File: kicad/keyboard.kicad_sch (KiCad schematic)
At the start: 74 parts, among them SW1 SW_MEC_5G, SW10 SW_MEC_5G, SW11 SW_MEC_5G, SW12 SW_MEC_5G, SW13 SW_MEC_5G, SW14 SW_MEC_5G, SW15 SW_MEC_5G, SW16 SW_MEC_5G, SW17 SW_MEC_5G, SW18 SW_MEC_5G, SW19 SW_MEC_5G, SW2 SW_MEC_5G, SW20 SW_MEC_5G, SW21 SW_MEC_5G, SW22 SW_MEC_5G, SW23 SW_MEC_5G, SW24 SW_MEC_5G, SW25 SW_MEC_5G, SW26 SW_MEC_5G, SW27 SW_MEC_5G, SW28 SW_MEC_5G, SW29 SW_MEC_5G, SW3 SW_MEC_5G, SW30 SW_MEC_5G, SW31 SW_MEC_5G, SW32 SW_MEC_5G, SW33 SW_MEC_5G, SW34 SW_MEC_5G, SW35 SW_MEC_5G, SW36 SW_MEC_5G, SW37 SW_MEC_5G, SW38 SW_MEC_5G, SW39 SW_MEC_5G, SW4 SW_MEC_5G, SW40 SW_MEC_5G, SW41 SW_MEC_5G, SW42 SW_MEC_5G, SW43 SW_MEC_5G, SW44 SW_MEC_5G, SW45 SW_MEC_5G, SW46 SW_MEC_5G, SW47 SW_MEC_5G, SW48 SW_MEC_5G, SW49 SW_MEC_5G, SW5 SW_MEC_5G, SW50 SW_MEC_5G, SW51 SW_MEC_5G, SW52 SW_MEC_5G, SW53 SW_MEC_5G, SW54 SW_MEC_5G, SW55 SW_MEC_5G, SW56 SW_MEC_5G, SW57 SW_MEC_5G, SW58 SW_MEC_5G, SW59 SW_MEC_5G, SW6 SW_MEC_5G, SW60 SW_MEC_5G, SW7 SW_MEC_5G, SW8 SW_MEC_5G, SW9 SW_MEC_5G, U1 MCP23017-E{slash}SO, U2 MCP23017-E{slash}SO, U3 MCP23017-E{slash}SO, U4 MCP23017-E{slash}SO

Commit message: Started on layout
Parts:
- A1: footprint pimoroni-boards_TINY2040 -> footprints:pimoroni-boards-TINY2040
- R2, R3: footprint (none) -> Resistor_SMD:R_0805_2012Metric_Pad1.20x1.40mm_HandSolder
- SW1, SW10, SW11, SW12, SW13, SW14, SW15, SW16, SW17, SW18, SW19, SW2, SW20, SW21, SW22, SW23, SW24, SW25, SW26, SW27, SW28, SW29, SW3, SW30, SW31, SW32, SW33, SW34, SW35, SW36, SW37, SW38, SW39, SW4, SW40, SW41, SW42, SW43, SW44, SW45, SW46, SW47, SW48, SW49, SW5, SW50, SW51, SW52, SW53, SW54, SW55, SW56, SW57, SW58, SW59, SW6, SW60, SW7, SW8, SW9: footprint (none) -> footprints:CherryMX_ChocV2_1u; symbol Switch:SW_MEC_5G -> project_library:SW_KAILH_CHOC_V2
- U1, U2, U3, U4: footprint SOIC127P1030X265-28N -> footprints:SOIC127P1030X265-28N
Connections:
- net GND: now also SW1.2 (B), SW10.2 (B), SW11.2 (B), SW12.2 (B), SW13.2 (B), SW14.2 (B), SW15.2 (B), SW16.2 (B), SW17.2 (B), SW18.2 (B), SW19.2 (B), SW2.2 (B), SW20.2 (B), SW21.2 (B), SW22.2 (B), SW23.2 (B), SW24.2 (B), SW25.2 (B), SW26.2 (B), SW27.2 (B), SW28.2 (B), SW29.2 (B), SW3.2 (B), SW30.2 (B), SW31.2 (B), SW32.2 (B), SW33.2 (B), SW34.2 (B), SW35.2 (B), SW36.2 (B), SW37.2 (B), SW38.2 (B), SW39.2 (B), SW4.2 (B), SW40.2 (B), SW41.2 (B), SW42.2 (B), SW43.2 (B), SW44.2 (B), SW45.2 (B), SW46.2 (B), SW47.2 (B), SW48.2 (B), SW49.2 (B), SW5.2 (B), SW50.2 (B), SW51.2 (B), SW52.2 (B), SW53.2 (B), SW54.2 (B), SW55.2 (B), SW56.2 (B), SW57.2 (B), SW58.2 (B), SW59.2 (B), SW6.2 (B), SW60.2 (B), SW7.2 (B), SW8.2 (B), SW9.2 (B); no longer SW1.3 (B), SW1.4 (B), SW10.3 (B), SW10.4 (B), SW11.3 (B), SW11.4 (B), SW12.3 (B), SW12.4 (B), SW13.3 (B), SW13.4 (B), SW14.3 (B), SW14.4 (B), SW15.3 (B), SW15.4 (B), SW16.3 (B), SW16.4 (B), SW17.3 (B), SW17.4 (B), SW18.3 (B), SW18.4 (B), SW19.3 (B), SW19.4 (B), SW2.3 (B), SW2.4 (B), SW20.3 (B), SW20.4 (B), SW21.3 (B), SW21.4 (B), SW22.3 (B), SW22.4 (B), SW23.3 (B), SW23.4 (B), SW24.3 (B), SW24.4 (B), SW25.3 (B), SW25.4 (B), SW26.3 (B), SW26.4 (B), SW27.3 (B), SW27.4 (B), SW28.3 (B), SW28.4 (B), SW29.3 (B), SW29.4 (B), SW3.3 (B), SW3.4 (B), SW30.3 (B), SW30.4 (B), SW31.3 (B), SW31.4 (B), SW32.3 (B), SW32.4 (B), SW33.3 (B), SW33.4 (B), SW34.3 (B), SW34.4 (B), SW35.3 (B), SW35.4 (B), SW36.3 (B), SW36.4 (B), SW37.3 (B), SW37.4 (B), SW38.3 (B), SW38.4 (B), SW39.3 (B), SW39.4 (B), SW4.3 (B), SW4.4 (B), SW40.3 (B), SW40.4 (B), SW41.3 (B), SW41.4 (B), SW42.3 (B), SW42.4 (B), SW43.3 (B), SW43.4 (B), SW44.3 (B), SW44.4 (B), SW45.3 (B), SW45.4 (B), SW46.3 (B), SW46.4 (B), SW47.3 (B), SW47.4 (B), SW48.3 (B), SW48.4 (B), SW49.3 (B), SW49.4 (B), SW5.3 (B), SW5.4 (B), SW50.3 (B), SW50.4 (B), SW51.3 (B), SW51.4 (B), SW52.3 (B), SW52.4 (B), SW53.3 (B), SW53.4 (B), SW54.3 (B), SW54.4 (B), SW55.3 (B), SW55.4 (B), SW56.3 (B), SW56.4 (B), SW57.3 (B), SW57.4 (B), SW58.3 (B), SW58.4 (B), SW59.3 (B), SW59.4 (B), SW6.3 (B), SW6.4 (B), SW60.3 (B), SW60.4 (B), SW7.3 (B), SW7.4 (B), SW8.3 (B), SW8.4 (B), SW9.3 (B), SW9.4 (B)
- net SW1: no longer SW1.2 (A)
- net SW10: no longer SW10.2 (A)
- net SW11: no longer SW11.2 (A)
- net SW12: no longer SW12.2 (A)
- net SW13: no longer SW13.2 (A)
- net SW14: no longer SW14.2 (A)
- net SW15: no longer SW15.2 (A)
- net SW16: no longer SW16.2 (A)
- net SW17: no longer SW17.2 (A)
- net SW18: no longer SW18.2 (A)
- net SW19: no longer SW19.2 (A)
- net SW2: no longer SW2.2 (A)
- net SW20: no longer SW20.2 (A)
- net SW21: no longer SW21.2 (A)
- net SW22: no longer SW22.2 (A)
- net SW23: no longer SW23.2 (A)
- net SW24: no longer SW24.2 (A)
- net SW25: no longer SW25.2 (A)
- net SW26: no longer SW26.2 (A)
- net SW27: no longer SW27.2 (A)
- net SW28: no longer SW28.2 (A)
- net SW29: no longer SW29.2 (A)
- net SW3: no longer SW3.2 (A)
- net SW30: no longer SW30.2 (A)
- net SW31: no longer SW31.2 (A)
- net SW32: no longer SW32.2 (A)
- net SW33: no longer SW33.2 (A)
- net SW34: no longer SW34.2 (A)
- net SW35: no longer SW35.2 (A)
- net SW36: no longer SW36.2 (A)
- net SW37: no longer SW37.2 (A)
- net SW38: no longer SW38.2 (A)
- net SW39: no longer SW39.2 (A)
- net SW4: no longer SW4.2 (A)
- net SW40: no longer SW40.2 (A)
- net SW41: no longer SW41.2 (A)
- net SW42: no longer SW42.2 (A)
- net SW43: no longer SW43.2 (A)
- net SW44: no longer SW44.2 (A)
- net SW45: no longer SW45.2 (A)
- net SW46: no longer SW46.2 (A)
- net SW47: no longer SW47.2 (A)
- net SW48: no longer SW48.2 (A)
- net SW49: no longer SW49.2 (A)
- net SW5: no longer SW5.2 (A)
- net SW50: no longer SW50.2 (A)
- net SW51: no longer SW51.2 (A)
- net SW52: no longer SW52.2 (A)
- net SW53: no longer SW53.2 (A)
- net SW54: no longer SW54.2 (A)
- net SW55: no longer SW55.2 (A)
- net SW56: no longer SW56.2 (A)
- net SW57: no longer SW57.2 (A)
- net SW58: no longer SW58.2 (A)
- net SW59: no longer SW59.2 (A)
- net SW6: no longer SW6.2 (A)
- net SW60: no longer SW60.2 (A)
- net SW7: no longer SW7.2 (A)
- net SW8: no longer SW8.2 (A)
- net SW9: no longer SW9.2 (A)

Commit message: WIP tracing
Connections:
- net SW2: now also U1.22 (GPA1); no longer U1.21 (GPA0)
- net SW4: now also U1.21 (GPA0); no longer U1.22 (GPA1)
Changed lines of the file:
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@@
     (effects (font (size 1.27 1.27)) (justify left bottom))
   )
-  (label "SW2" (at 63.5 45.72 0)
+  (label "SW2" (at 63.5 48.26 0)
     (effects (font (size 1.27 1.27)) (justify left bottom))
   )
@@
     (effects (font (size 1.27 1.27)) (justify right bottom))
   )
-  (label "SW4" (at 63.5 48.26 0)
-    (effects (font (size 1.27 1.27)) (justify left bottom))
-  )
+  (label "SW4" (at 63.5 45.72 0)
+    (effects (font (size 1.27 1.27)) (justify left bottom))
+  )

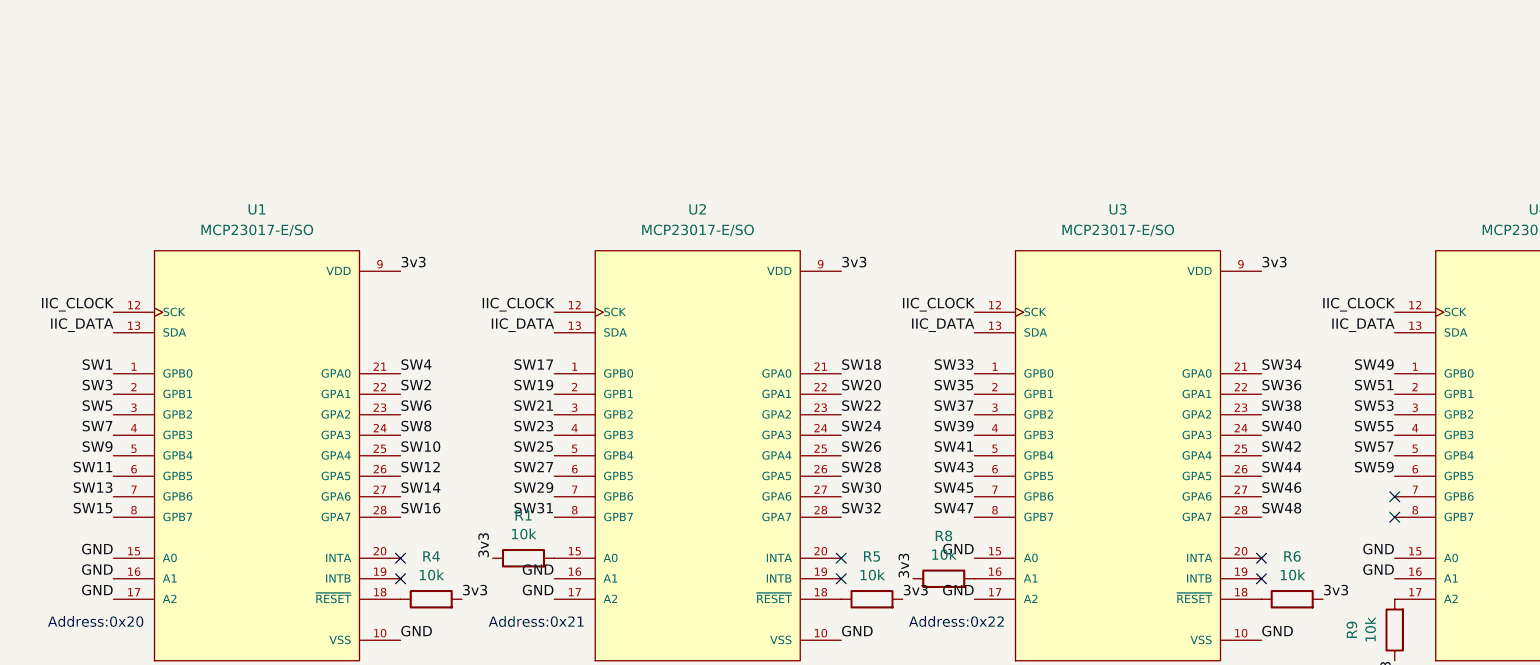
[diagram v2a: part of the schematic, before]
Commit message: Reordered switch pins and re-traced
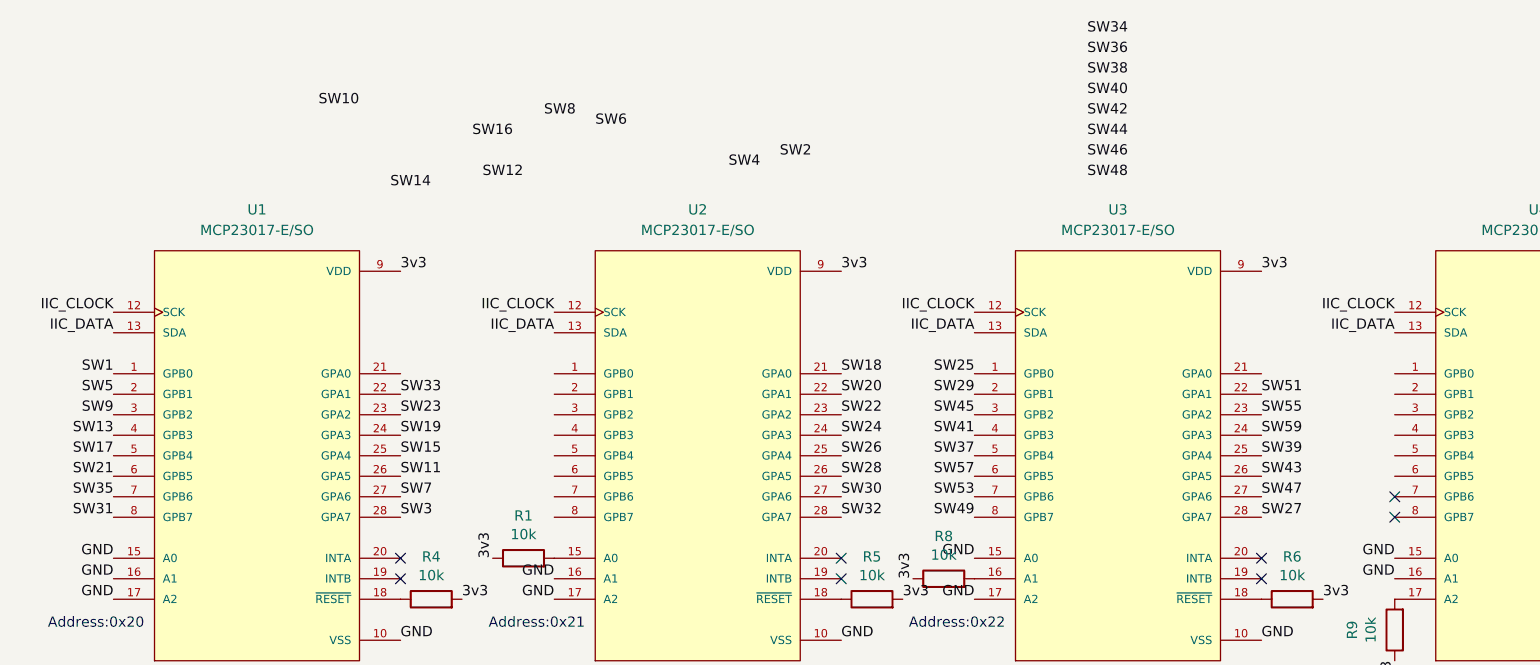
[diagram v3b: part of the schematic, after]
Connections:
- net SW10: no longer U1.25 (GPA4)
- net SW11: now also U1.26 (GPA5); no longer U1.6 (GPB5)
- net SW12: no longer U1.26 (GPA5)
- net SW13: now also U1.4 (GPB3); no longer U1.7 (GPB6)
- net SW14: no longer U1.27 (GPA6)
- net SW15: now also U1.25 (GPA4); no longer U1.8 (GPB7)
- net SW16: no longer U1.28 (GPA7)
- net SW17: now also U1.5 (GPB4); no longer U2.1 (GPB0)
- net SW19: now also U1.24 (GPA3); no longer U2.2 (GPB1)
- net SW2: no longer U1.22 (GPA1)
- net SW21: now also U1.6 (GPB5); no longer U2.3 (GPB2)
- net SW23: now also U1.23 (GPA2); no longer U2.4 (GPB3)
- net SW25: now also U3.1 (GPB0); no longer U2.5 (GPB4)
- net SW27: now also U3.28 (GPA7); no longer U2.6 (GPB5)
- net SW29: now also U3.2 (GPB1); no longer U2.7 (GPB6)
- net SW3: now also U1.28 (GPA7); no longer U1.2 (GPB1)
- net SW31: now also U1.8 (GPB7); no longer U2.8 (GPB7)
- net SW33: now also U1.22 (GPA1); no longer U3.1 (GPB0)
- net SW34: no longer U3.21 (GPA0)
- net SW35: now also U1.7 (GPB6); no longer U3.2 (GPB1)
- net SW36: no longer U3.22 (GPA1)
- net SW37: now also U3.5 (GPB4); no longer U3.3 (GPB2)
- net SW38: no longer U3.23 (GPA2)
- net SW39: now also U3.25 (GPA4); no longer U3.4 (GPB3)
- net SW4: no longer U1.21 (GPA0)
- net SW40: no longer U3.24 (GPA3)
- net SW41: now also U3.4 (GPB3); no longer U3.5 (GPB4)
- net SW42: no longer U3.25 (GPA4)
- net SW43: now also U3.26 (GPA5); no longer U3.6 (GPB5)
- net SW44: no longer U3.26 (GPA5)
- net SW45: now also U3.3 (GPB2); no longer U3.7 (GPB6)
- net SW46: no longer U3.27 (GPA6)
- net SW47: now also U3.27 (GPA6); no longer U3.8 (GPB7)
- net SW48: no longer U3.28 (GPA7)
- net SW49: now also U3.8 (GPB7); no longer U4.1 (GPB0)
- net SW5: now also U1.2 (GPB1); no longer U1.3 (GPB2)
- net SW51: now also U3.22 (GPA1); no longer U4.2 (GPB1)
- net SW53: now also U3.7 (GPB6); no longer U4.3 (GPB2)
- net SW55: now also U3.23 (GPA2); no longer U4.4 (GPB3)
- net SW57: now also U3.6 (GPB5); no longer U4.5 (GPB4)
- net SW59: now also U3.24 (GPA3); no longer U4.6 (GPB5)
- net SW6: no longer U1.23 (GPA2)
- net SW7: now also U1.27 (GPA6); no longer U1.4 (GPB3)
- net SW8: no longer U1.24 (GPA3)
- net SW9: now also U1.3 (GPB2); no longer U1.5 (GPB4)

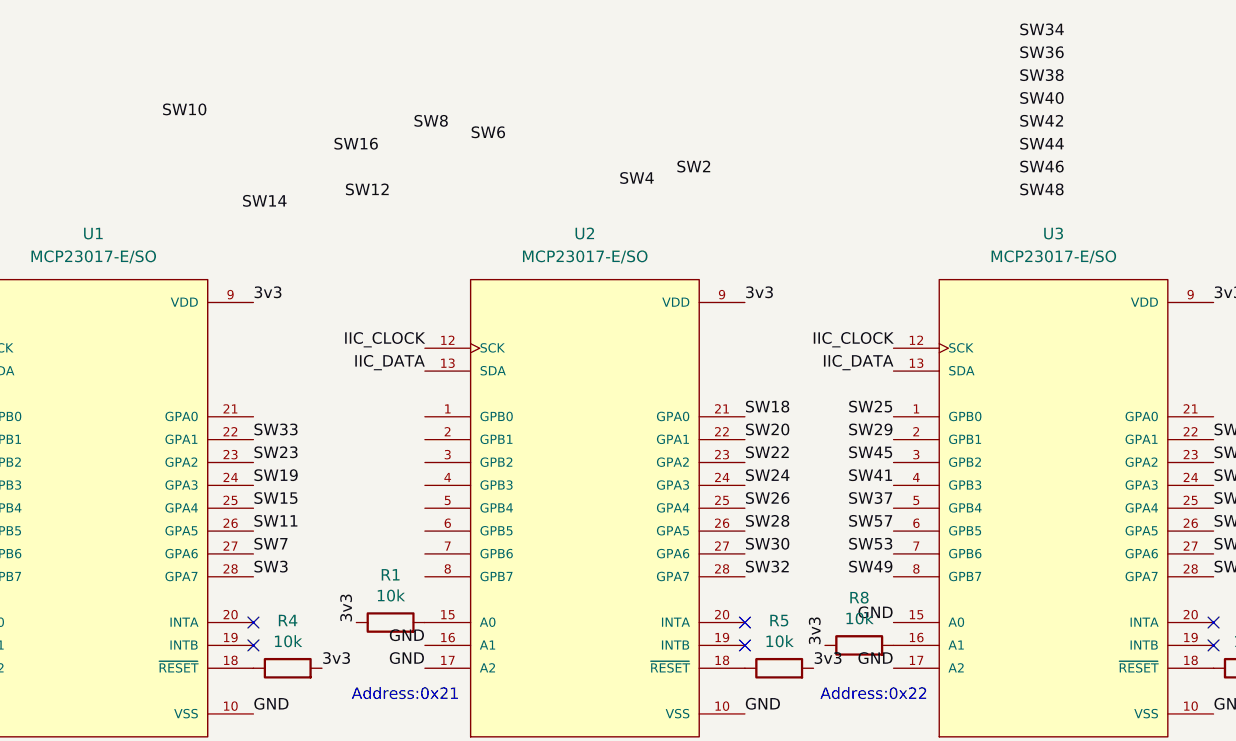
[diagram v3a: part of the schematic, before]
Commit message: Reordered switch pins and re-traced
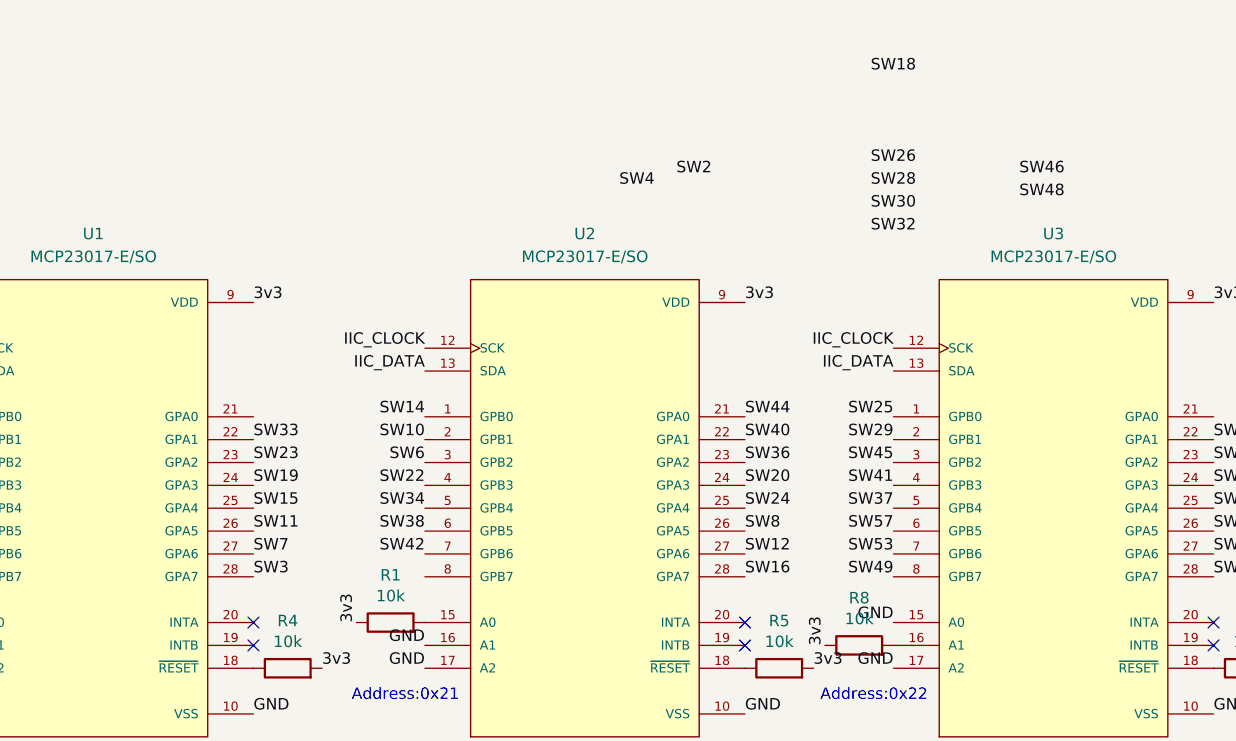
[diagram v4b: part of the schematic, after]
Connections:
- net SW10: now also U2.2 (GPB1)
- net SW12: now also U2.27 (GPA6)
- net SW14: now also U2.1 (GPB0)
- net SW16: now also U2.28 (GPA7)
- net SW18: no longer U2.21 (GPA0)
- net SW20: now also U2.24 (GPA3); no longer U2.22 (GPA1)
- net SW22: now also U2.4 (GPB3); no longer U2.23 (GPA2)
- net SW24: now also U2.25 (GPA4); no longer U2.24 (GPA3)
- net SW26: no longer U2.25 (GPA4)
- net SW28: no longer U2.26 (GPA5)
- net SW30: no longer U2.27 (GPA6)
- net SW32: no longer U2.28 (GPA7)
- net SW34: now also U2.5 (GPB4)
- net SW36: now also U2.23 (GPA2)
- net SW38: now also U2.6 (GPB5)
- net SW40: now also U2.22 (GPA1)
- net SW42: now also U2.7 (GPB6)
- net SW44: now also U2.21 (GPA0)
- net SW6: now also U2.3 (GPB2)
- net SW8: now also U2.26 (GPA5)
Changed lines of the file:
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@@
     (effects (font (size 1.27 1.27)) (justify right bottom))
   )
-  (label "SW30" (at 118.11 60.96 0)
+  (label "SW30" (at 132.08 22.86 0)
     (effects (font (size 1.27 1.27)) (justify left bottom))
   )
@@
     (effects (font (size 1.27 1.27)) (justify left bottom))
   )
-  (label "SW10" (at 53.34 12.7 0)
-    (effects (font (size 1.27 1.27)) (justify left bottom))
+  (label "SW10" (at 82.55 48.26 180)
+    (effects (font (size 1.27 1.27)) (justify right bottom))
   )
   (label "GND" (at 27.94 73.66 180)
@@
     (effects (font (size 1.27 1.27)) (justify right bottom))
   )
-  (label "SW6" (at 87.63 15.24 0)
-    (effects (font (size 1.27 1.27)) (justify left bottom))
-  )
-  (label "SW24" (at 118.11 53.34 0)
+  (label "SW6" (at 82.55 50.8 180)
+    (effects (font (size 1.27 1.27)) (justify right bottom))
+  )
+  (label "SW24" (at 118.11 55.88 0)
     (effects (font (size 1.27 1.27)) (justify left bottom))
   )
@@
     (effects (font (size 1.27 1.27)) (justify right bottom))
   )
-  (label "SW34" (at 148.59 3.81 0)
-    (effects (font (size 1.27 1.27)) (justify left bottom))
+  (label "SW34" (at 82.55 55.88 180)
+    (effects (font (size 1.27 1.27)) (justify right bottom))
   )
   (label "3v3" (at 273.05 13.97 0)
@@
     (effects (font (size 1.27 1.27)) (justify right bottom))
   )
-  (label "SW28" (at 118.11 58.42 0)
+  (label "SW28" (at 132.08 20.32 0)
     (effects (font (size 1.27 1.27)) (justify left bottom))
   )
@@
     (effects (font (size 1.27 1.27)) (justify right bottom))
   )
-  (label "SW8" (at 81.28 13.97 0)
+  (label "SW8" (at 118.11 58.42 0)
     (effects (font (size 1.27 1.27)) (justify left bottom))
   )
@@
     (effects (font (size 1.27 1.27)) (justify right bottom))
   )
-  (label "SW42" (at 148.59 13.97 0)
-    (effects (font (size 1.27 1.27)) (justify left bottom))
+  (label "SW42" (at 82.55 60.96 180)
+    (effects (font (size 1.27 1.27)) (justify right bottom))
   )
   (label "IIC_DATA" (at 27.94 40.64 180)
@@
     (effects (font (size 1.27 1.27)) (justify right bottom))
   )
-  (label "SW32" (at 118.11 63.5 0)
+  (label "SW32" (at 132.08 25.4 0)
     (effects (font (size 1.27 1.27)) (justify left bottom))
   )
@@
     (effects (font (size 1.27 1.27)) (justify left bottom))
   )
-  (label "SW22" (at 118.11 50.8 0)
-    (effects (font (size 1.27 1.27)) (justify left bottom))
+  (label "SW22" (at 82.55 53.34 180)
+    (effects (font (size 1.27 1.27)) (justify right bottom))
   )
   (label "SW1" (at 27.94 45.72 180)
@@
     (effects (font (size 1.27 1.27)) (justify right bottom))
   )
-  (label "SW18" (at 118.11 45.72 0)
+  (label "SW18" (at 132.08 7.62 0)
     (effects (font (size 1.27 1.27)) (justify left bottom))
   )
@@
     (effects (font (size 1.27 1.27)) (justify right bottom))
   )
-  (label "SW26" (at 118.11 55.88 0)
+  (label "SW26" (at 132.08 17.78 0)
     (effects (font (size 1.27 1.27)) (justify left bottom))
   )
@@
     (effects (font (size 1.27 1.27)) (justify right bottom))
   )
-  (label "SW36" (at 148.59 6.35 0)
+  (label "SW36" (at 118.11 50.8 0)
     (effects (font (size 1.27 1.27)) (justify left bottom))
   )
@@
     (effects (font (size 1.27 1.27)) (justify right bottom))
   )
-  (label "SW16" (at 72.39 16.51 0)
+  (label "SW16" (at 118.11 63.5 0)
     (effects (font (size 1.27 1.27)) (justify left bottom))
   )
@@
     (effects (font (size 1.27 1.27)) (justify left bottom))
   )
-  (label "SW44" (at 148.59 16.51 0)
+  (label "SW44" (at 118.11 45.72 0)
     (effects (font (size 1.27 1.27)) (justify left bottom))
   )
@@
     (effects (font (size 1.27 1.27)) (justify right bottom))
   )
-  (label "SW40" (at 148.59 11.43 0)
+  (label "SW40" (at 118.11 48.26 0)
     (effects (font (size 1.27 1.27)) (justify left bottom))
   )
@@
     (effects (font (size 1.27 1.27)) (justify right bottom))
   )
-  (label "SW14" (at 62.23 22.86 0)
-    (effects (font (size 1.27 1.27)) (justify left bottom))
+  (label "SW14" (at 82.55 45.72 180)
+    (effects (font (size 1.27 1.27)) (justify right bottom))
   )
   (label "IIC_DATA" (at 186.69 40.64 180)
@@
     (effects (font (size 1.27 1.27)) (justify right bottom))
   )
-  (label "SW38" (at 148.59 8.89 0)
-    (effects (font (size 1.27 1.27)) (justify left bottom))
+  (label "SW38" (at 82.55 58.42 180)
+    (effects (font (size 1.27 1.27)) (justify right bottom))
   )
   (label "3v3" (at 71.12 73.66 0)
@@
     (effects (font (size 1.27 1.27)) (justify right bottom))
   )
-  (label "SW12" (at 73.66 21.59 0)
+  (label "SW12" (at 118.11 60.96 0)
     (effects (font (size 1.27 1.27)) (justify left bottom))
   )
@@
     (effects (font (size 1.27 1.27)) (justify right bottom))
   )
-  (label "SW20" (at 118.11 48.26 0)
-    (effects (font (size 1.27 1.27)) (justify left bottom))
-  )
+  (label "SW20" (at 118.11 53.34 0)
+    (effects (font (size 1.27 1.27)) (justify left bottom))
+  )
